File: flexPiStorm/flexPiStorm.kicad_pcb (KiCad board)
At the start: 2 copper layers, 32 x 103 mm, 16 parts, among them J1 Conn_01x04, J2 FPC-FFC-64, U1 MC68000

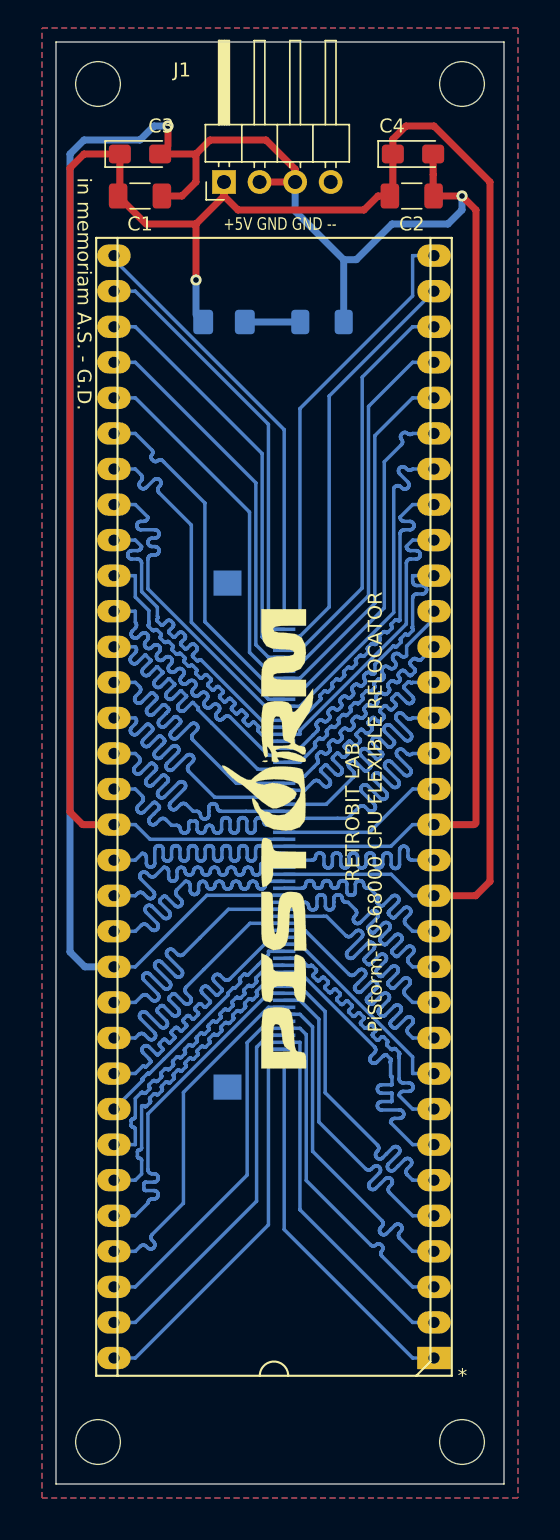
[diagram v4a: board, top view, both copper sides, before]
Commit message: Inverted ffc/fpc pinout for reverse mounting. Cable must be SAME SIDE
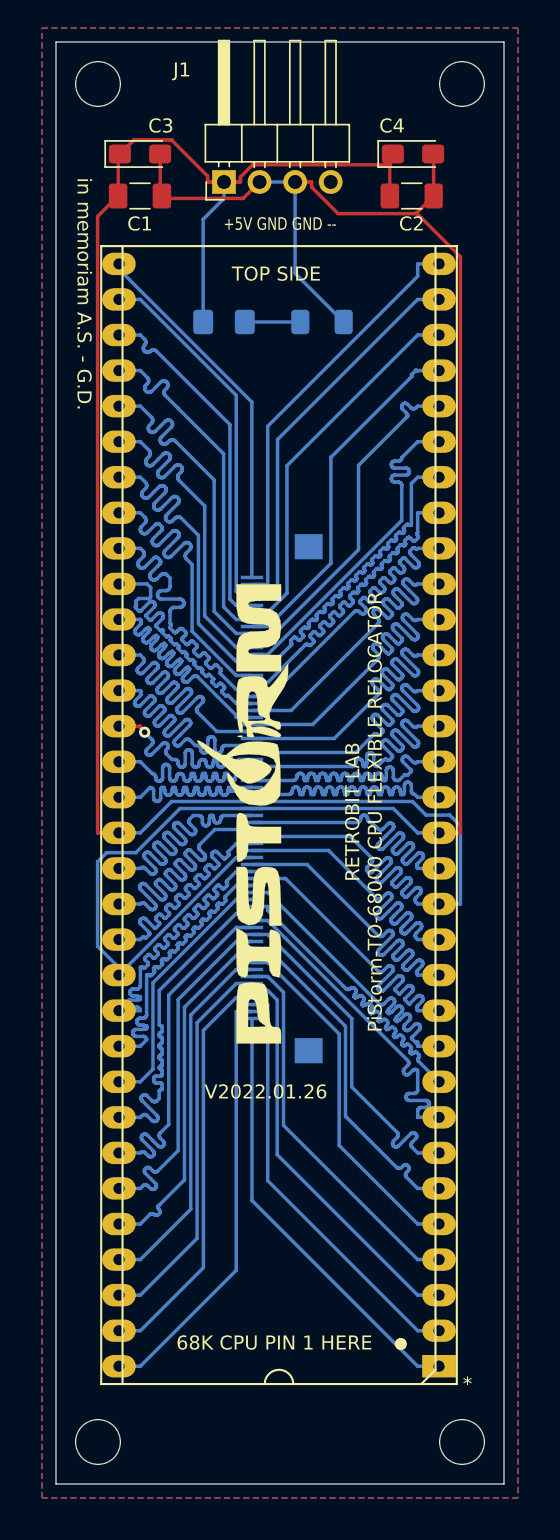
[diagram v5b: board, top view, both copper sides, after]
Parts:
- moved J2 3.55 mm to (139.0, 100.0), turned to 270 degrees
- moved L3 2.52 mm to (138.2, 101.2)
- moved U1 0.69 mm to (152.4, 140.6)
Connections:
- J2 pad 1: /P1 -> /P64
- J2 pad 10: /P10 -> /P55
- J2 pad 11: /P11 -> /P54
- J2 pad 12: /P12 -> /P53
- J2 pad 13: /P13 -> /P52
- J2 pad 14: /P14 -> /P51
- J2 pad 15: /P15 -> /P50
- J2 pad 16: /P16 -> /P49
- J2 pad 17: /P17 -> /P48
- J2 pad 18: /P18 -> /P47
- J2 pad 19: /P19 -> /P46
- J2 pad 2: /P2 -> /P63
- J2 pad 20: /P20 -> /P45
- J2 pad 21: /P21 -> /P44
- J2 pad 22: /P22 -> /P43
- J2 pad 23: /P23 -> /P42
- J2 pad 24: GND -> /P41
- J2 pad 25: /P25 -> /P40
- J2 pad 26: /P26 -> /P39
- J2 pad 27: VCC -> /P38
- J2 pad 28: /P28 -> /P37
- J2 pad 29: /P29 -> /P36
- J2 pad 3: /P3 -> /P62
- J2 pad 30: /P30 -> /P35
- J2 pad 31: GND -> /P34
- J2 pad 32: VCC -> /P33
- J2 pad 33: /P33 -> VCC
- J2 pad 34: /P34 -> GND
- J2 pad 35: /P35 -> /P30
- J2 pad 36: /P36 -> /P29
- J2 pad 37: /P37 -> /P28
- J2 pad 38: /P38 -> VCC
- J2 pad 39: /P39 -> /P26
- J2 pad 4: /P4 -> /P61
- J2 pad 40: /P40 -> /P25
- J2 pad 41: /P41 -> GND
- J2 pad 42: /P42 -> /P23
- J2 pad 43: /P43 -> /P22
- J2 pad 44: /P44 -> /P21
- J2 pad 45: /P45 -> /P20
- J2 pad 46: /P46 -> /P19
- J2 pad 47: /P47 -> /P18
- J2 pad 48: /P48 -> /P17
- J2 pad 49: /P49 -> /P16
- J2 pad 5: /P5 -> /P60
- J2 pad 50: /P50 -> /P15
- J2 pad 51: /P51 -> /P14
- J2 pad 52: /P52 -> /P13
- J2 pad 53: /P53 -> /P12
- J2 pad 54: /P54 -> /P11
- J2 pad 55: /P55 -> /P10
- J2 pad 56: /P56 -> /P9
- J2 pad 57: /P57 -> /P8
- J2 pad 58: /P58 -> /P7
- J2 pad 59: /P59 -> /P6
- J2 pad 6: /P6 -> /P59
- J2 pad 60: /P60 -> /P5
- J2 pad 61: /P61 -> /P4
- J2 pad 62: /P62 -> /P3
- J2 pad 63: /P63 -> /P2
- J2 pad 64: /P64 -> /P1
- J2 pad 7: /P7 -> /P58
- J2 pad 8: /P8 -> /P57
- J2 pad 9: /P9 -> /P56
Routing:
- net GND: track 192.6 -> 134.5 mm, vias 2 -> 0
- net VCC: track 178.1 -> 145.0 mm, vias 1 -> 0
- net /P33: track 12.0 -> 25.1 mm
- net /P17: track 15.2 -> 25.1 mm
- net /P16: track 17.5 -> 25.5 mm
- net /P36: track 25.0 -> 17.4 mm
- net /P38: track 25.0 -> 18.0 mm, vias 0 -> 1
- net /P18: track 25.2 -> 18.5 mm
- net /P43: track 19.1 -> 25.5 mm
- net /P41: track 19.8 -> 25.5 mm
- net /P25: track 19.9 -> 25.5 mm
- net /P34: track 23.9 -> 18.4 mm
- net /P29: track 20.5 -> 25.1 mm
- net /P28: track 21.0 -> 25.6 mm
- net /P3: track 26.0 -> 30.4 mm
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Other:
- board text added: "68K CPU PIN 1 HERE"
- board text added: "BOTTOM SIDE"
- board text added: "TOP SIDE"
- board text added: "V2022.01.26"

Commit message: Modified as requested by JLCPCB with e-mail in beginning of Feb. 2022 (Tracks too small)
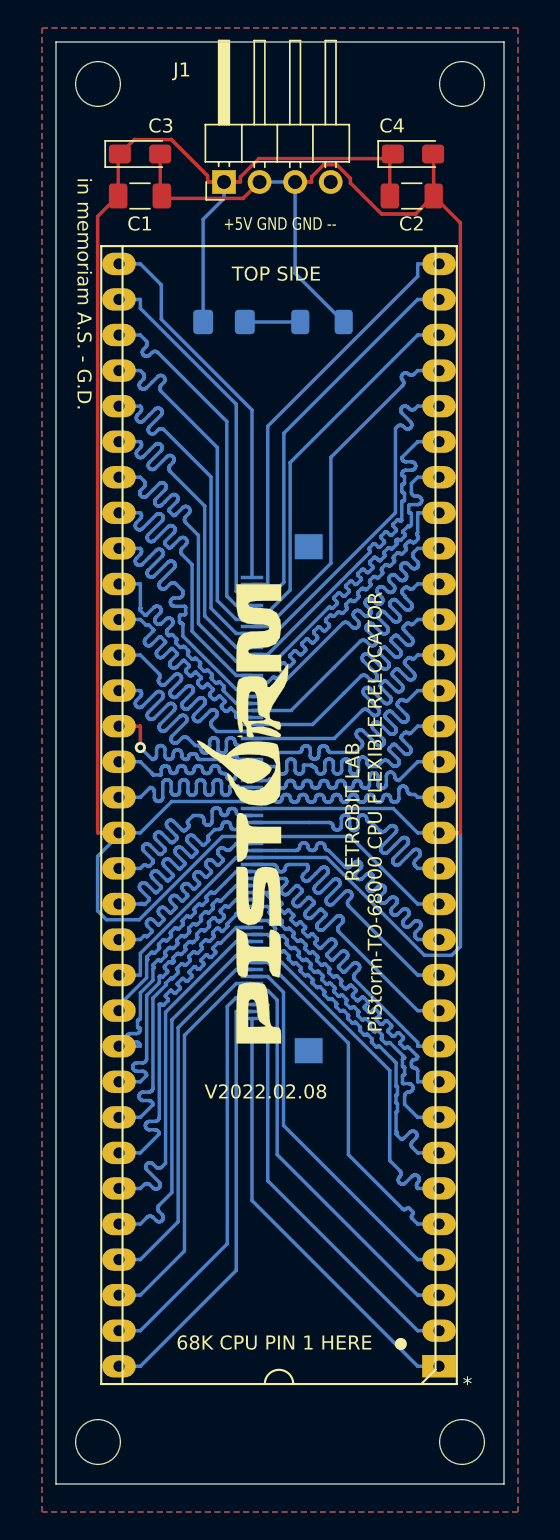
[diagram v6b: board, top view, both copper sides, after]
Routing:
- net VCC: track 145.0 -> 132.3 mm
- net GND: track 134.5 -> 143.8 mm
- net /P22: track 25.0 -> 16.2 mm
- net /P33: track 25.1 -> 19.6 mm
- net /P35: track 25.1 -> 20.6 mm
- net /P30: track 25.1 -> 20.7 mm
- net /P36: track 17.4 -> 13.1 mm
- net /P18: track 18.5 -> 22.6 mm
- net /P42: track 25.5 -> 21.6 mm
- net /P44: track 25.1 -> 21.4 mm
- net /P38: track 18.0 -> 14.6 mm
- net /P46: track 21.5 -> 18.7 mm
- net /P20: track 22.7 -> 20.3 mm
- net /P28: track 25.6 -> 23.3 mm
- net /P16: track 25.5 -> 23.3 mm
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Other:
- board text added: "V2022.02.08"
- board text removed: "V2022.01.26"
